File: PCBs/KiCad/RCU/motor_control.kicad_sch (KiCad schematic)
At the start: 36 parts, among them J300 Right_Motor_Screw_Terminal, J301 Right_Encoder_Conn, J302 Left_Motor_Screw_Terminal, J303 Left_Encoder_Conn, U300 OPA320, U301 DRV8876, U302 OPA320, U303 DRV8876

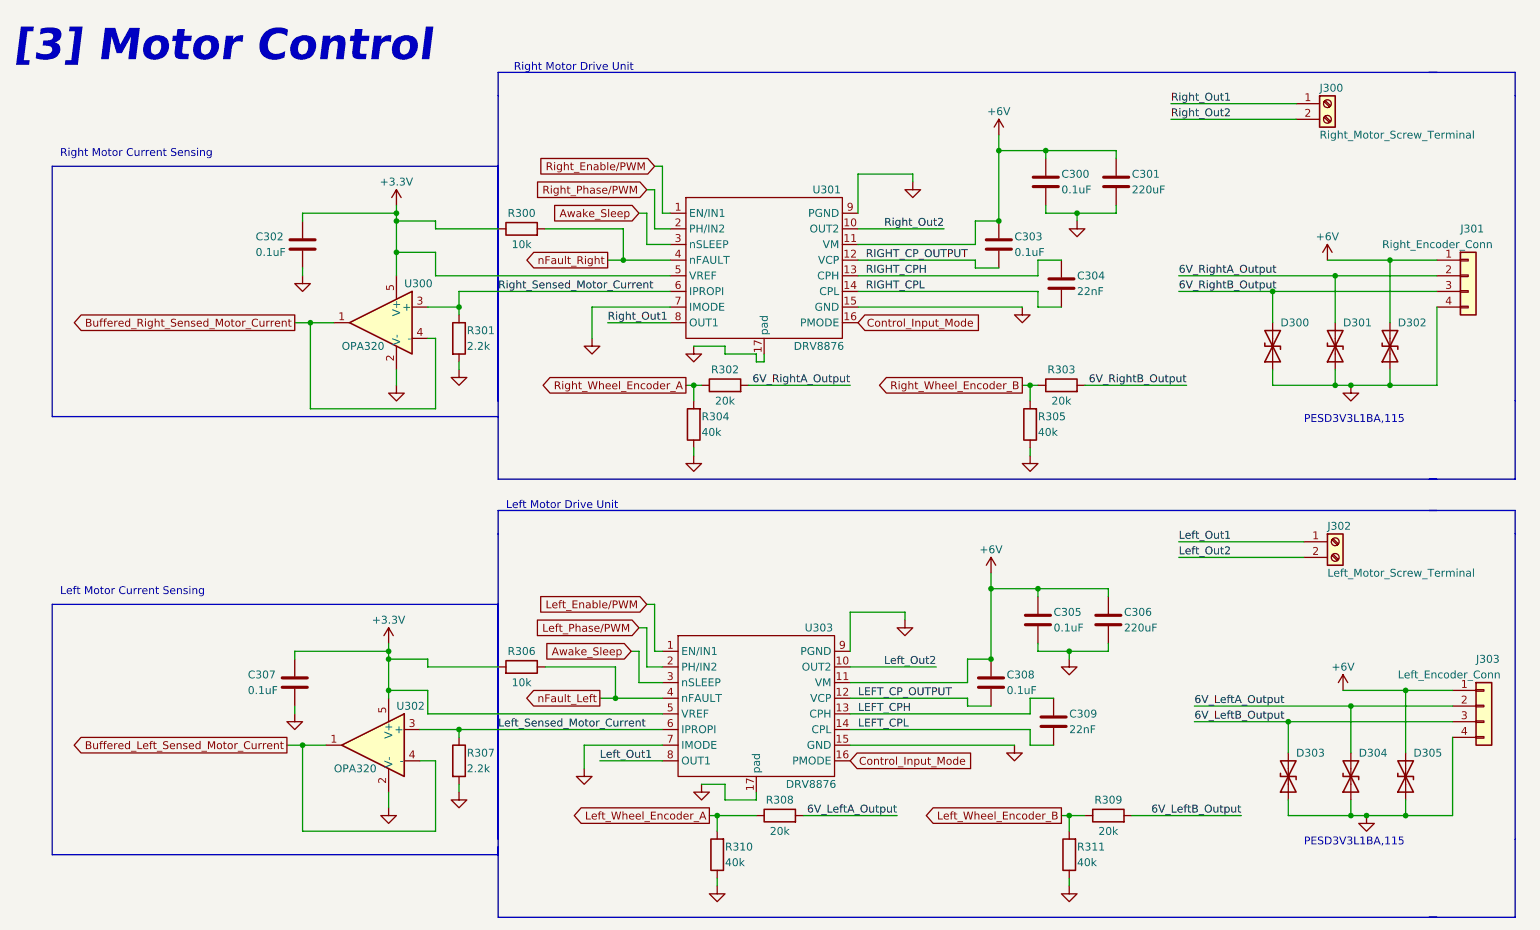
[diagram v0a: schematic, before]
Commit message: Moved project library one folder up to Kicad Folder
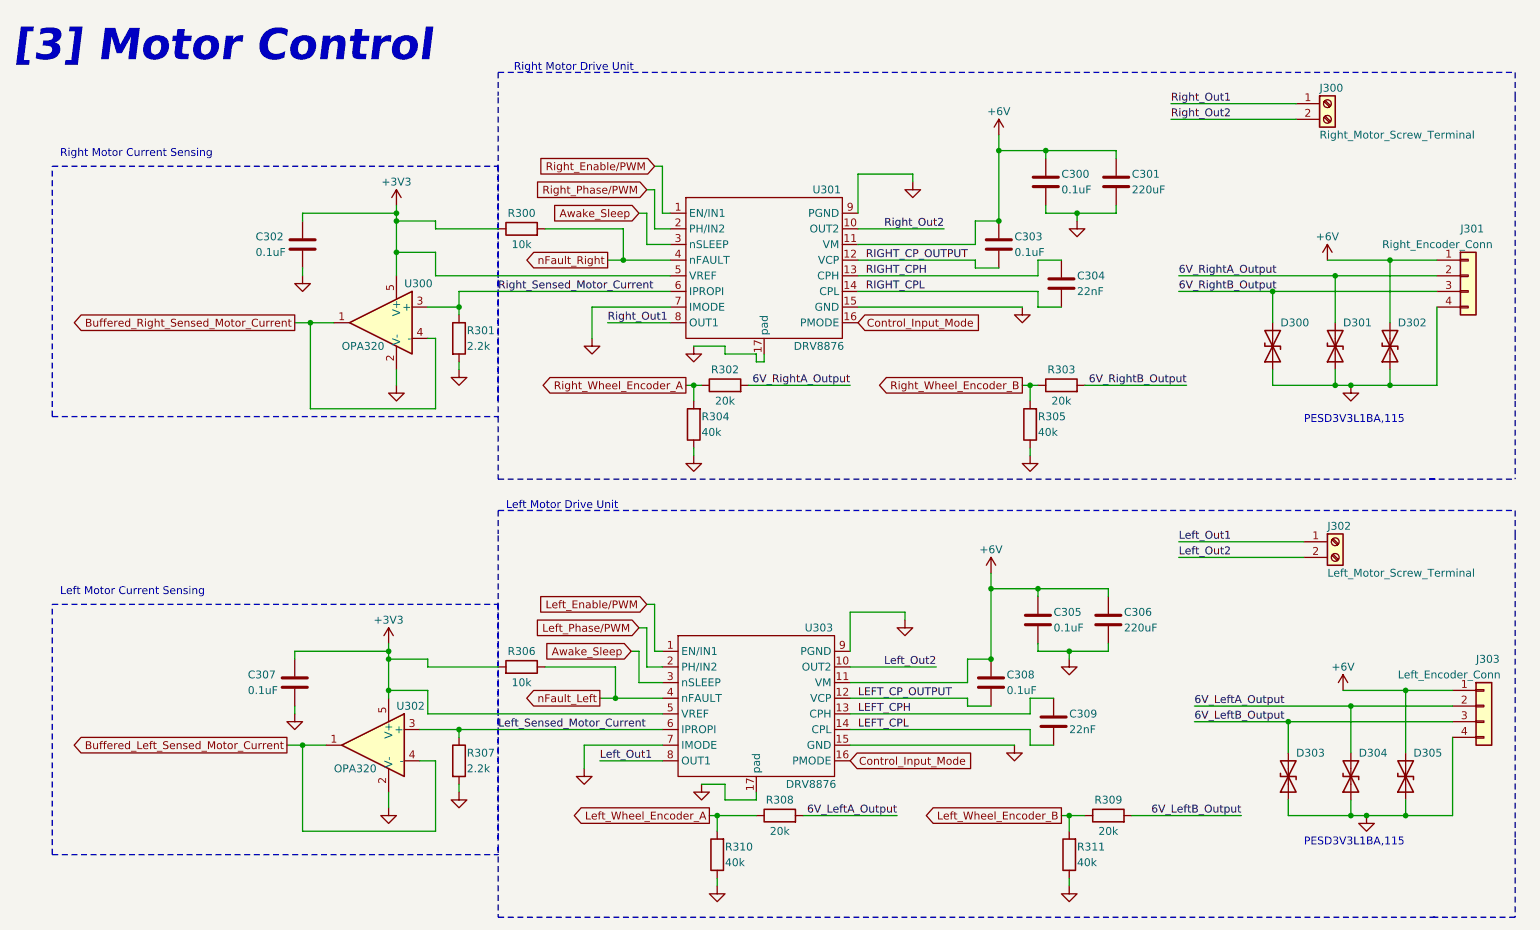
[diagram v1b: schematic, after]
